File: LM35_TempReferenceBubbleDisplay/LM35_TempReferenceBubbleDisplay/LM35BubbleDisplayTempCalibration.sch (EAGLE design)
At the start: 26 parts, among them IC1 ATMEGA328-20P, U1 SN74HC595N, Y1 16MHz

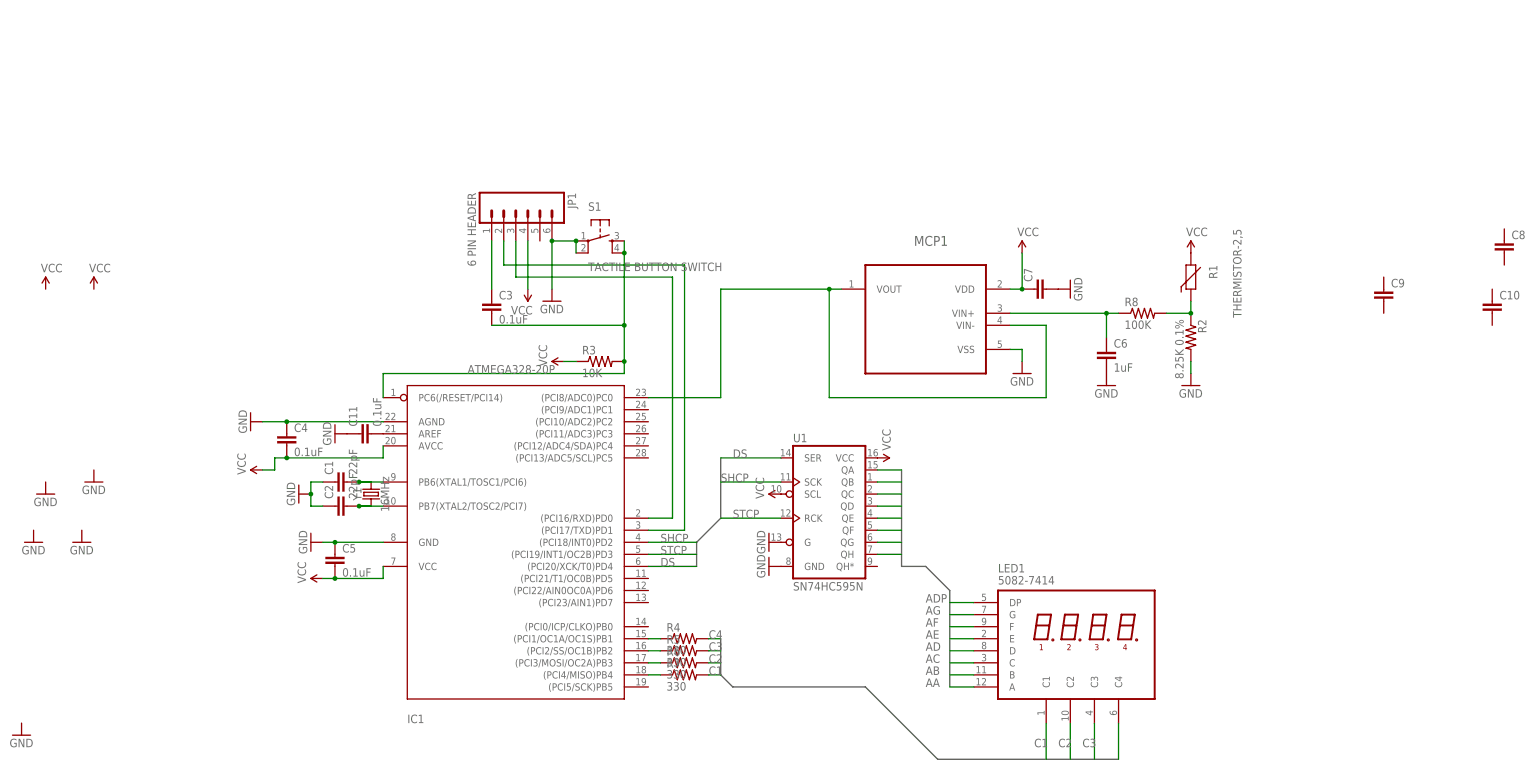
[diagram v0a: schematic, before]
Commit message: Added a JobList to outline jobs completed, to be completed and known bugs. Added schematic to show connections for LM35 temperature sensor used for calibration of the thermistor sensing circuitry. Removed extra folder of Thermistor4c for Bubble Display
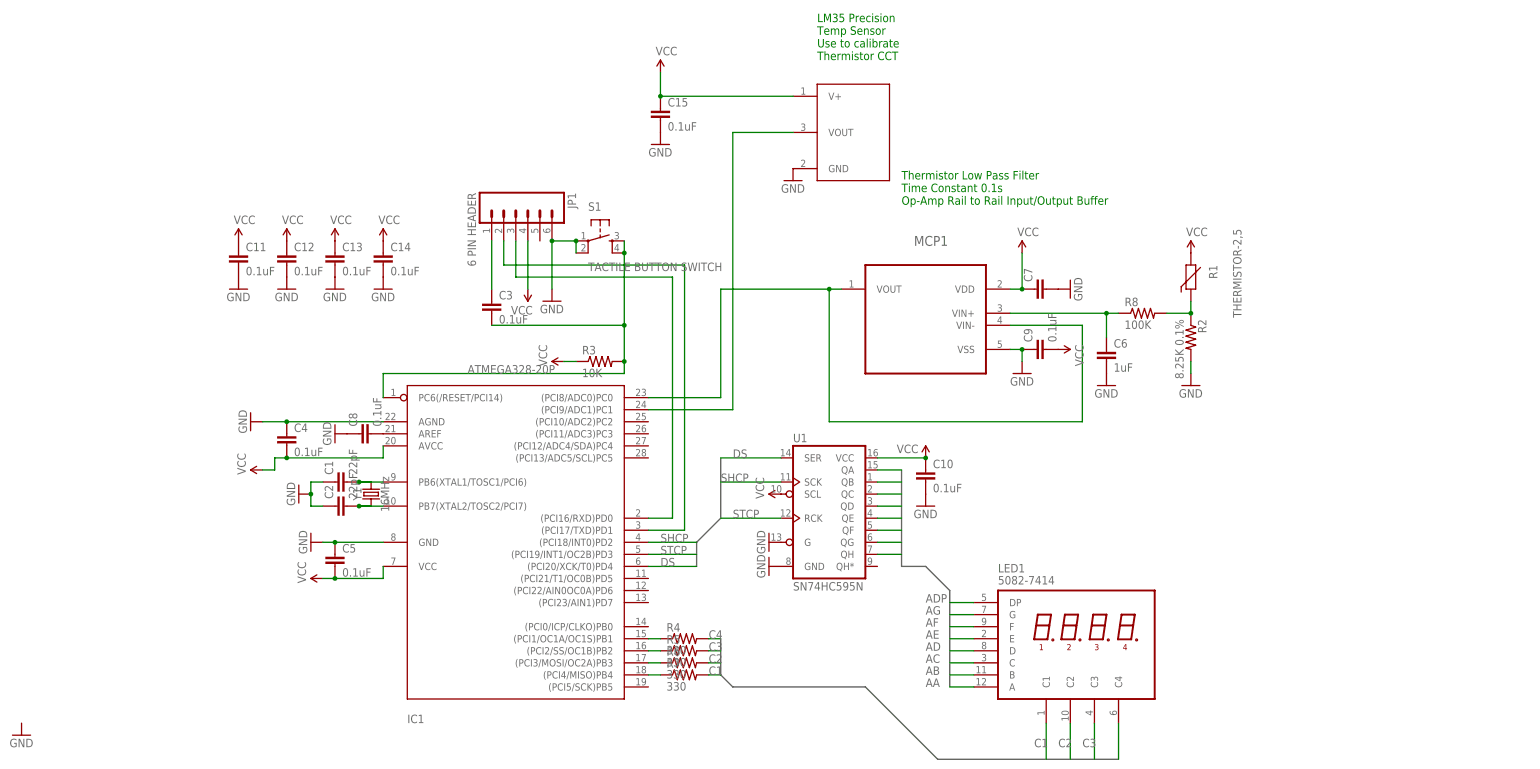
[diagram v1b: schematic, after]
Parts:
- added C12, C13, C14, C15: 0.1uF, SparkFun-Capacitors:CAPEZ
- added U$1: (no value), RossParts:LM35
- C10, C8, C9: value (none) -> 0.1uF
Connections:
- new net N$15: IC1.(PCI9/ADC1)PC1, U$1.VOUT
- net GND: now also C10.2, C11.2, C12.2, C13.2, C14.2, C15.2, C8.1, C9.1, U$1.GND; no longer C11.1
- net N$4: now also C8.2; no longer C11.2
- net VCC: now also C10.1, C11.1, C12.1, C13.1, C14.1, C15.1, C9.2, U$1.V+
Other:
- note added: "LM35 Precision Temp Sensor Use to calibrate Thermistor CCT"
- note added: "Thermistor Low Pass Filter Time Constant 0.1s Op-Amp Rail to Rail Input/Output Buffer"
- moved on the sheet: C10, C11, C8, C9
